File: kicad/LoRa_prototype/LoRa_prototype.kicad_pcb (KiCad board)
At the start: 4 copper layers, 100 x 90 mm, 138 parts, among them J1 Conn_ST_STDC14, J10 SYS, J11 BME, J12 GPS, J14 SPI_FLASH, J15 SYS, J18 MCO, J2 USB_C_Receptacle_PowerOnly_6P, J3 BAT, J4 SMA Female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

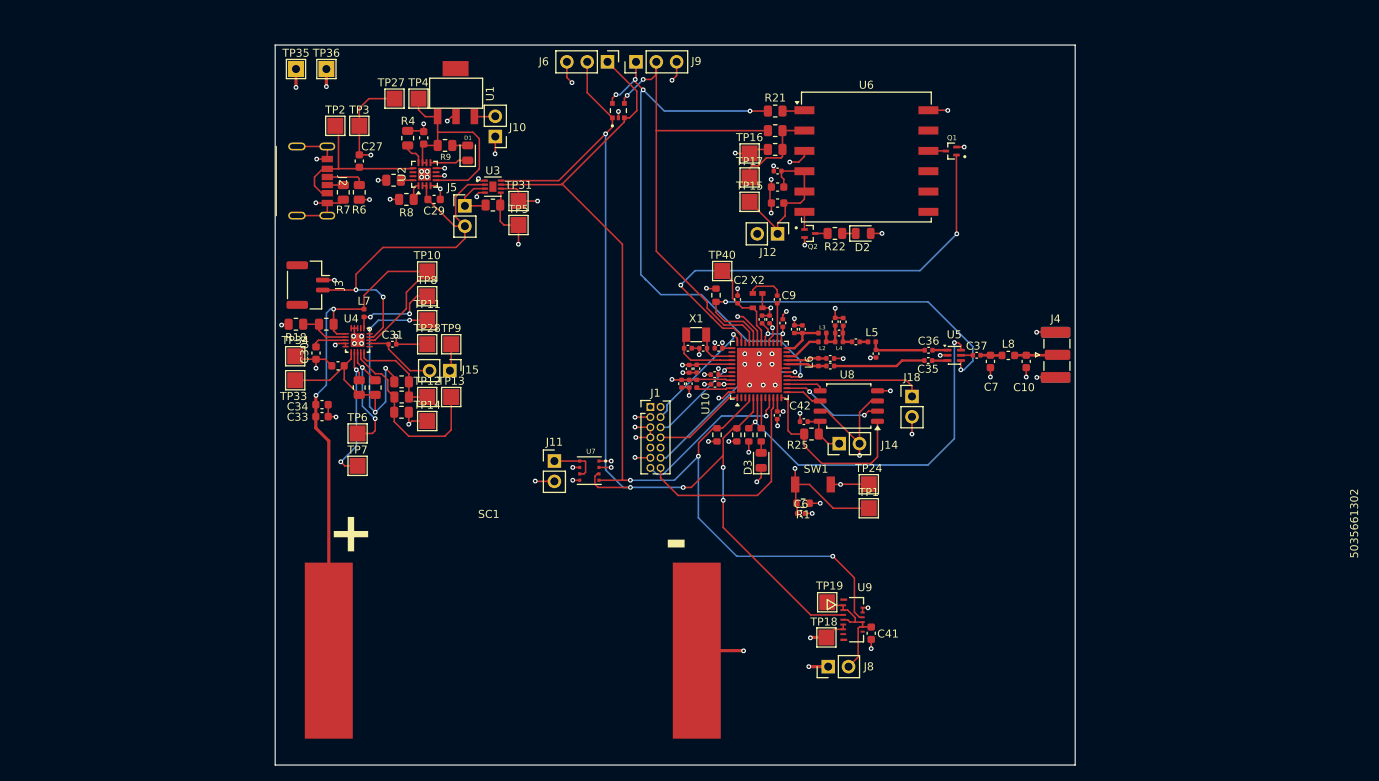
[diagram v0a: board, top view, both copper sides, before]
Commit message: Prettified silkscreen layer
0 errors and 33 warnings in DRC
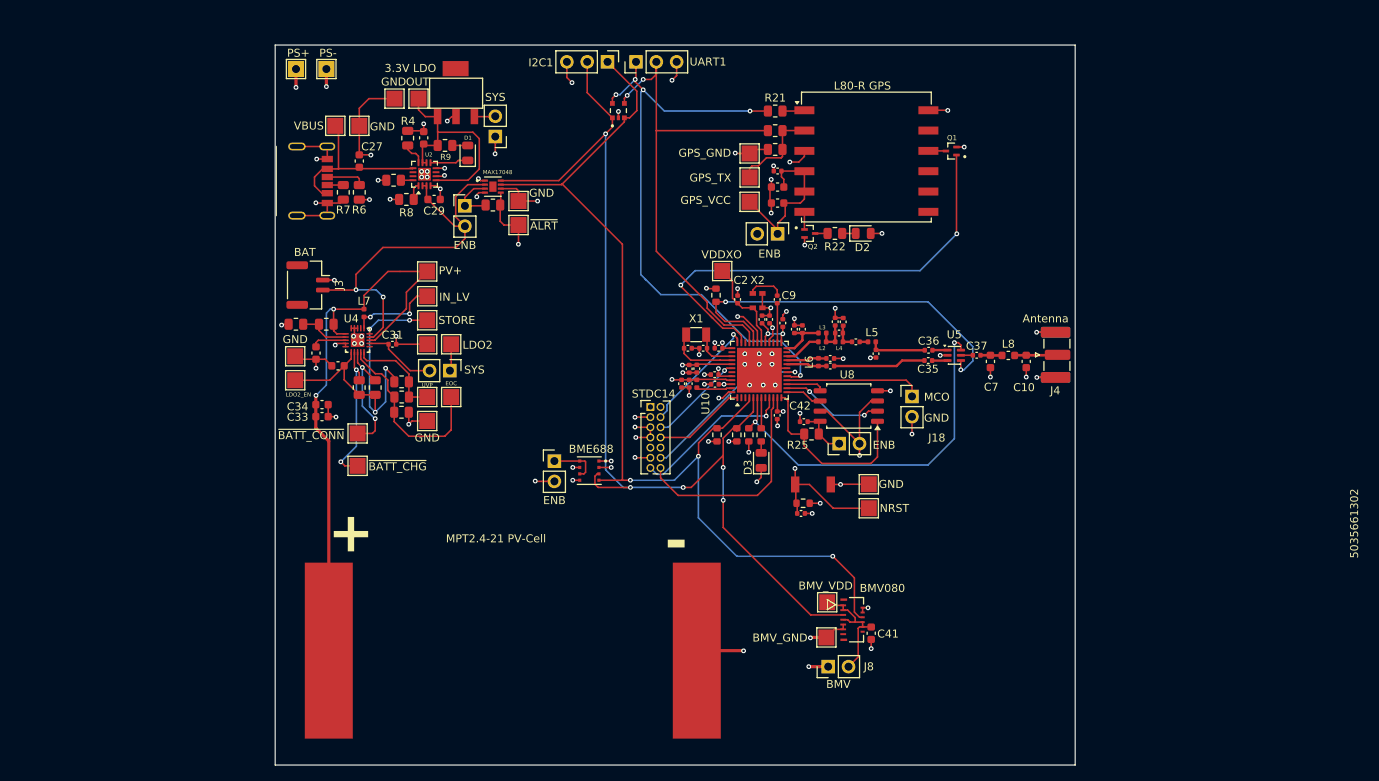
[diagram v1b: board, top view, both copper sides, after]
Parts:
- J1: value Conn_ST_STDC14 -> STDC14
- J11: value BME -> ENB
- J12: value GPS -> ENB
- J14: value SPI_FLASH -> ENB
- J4: value SMA Female -> Antenna
- J5: value FG -> ENB
- SC1: value PV_Cell -> MPT2.4-21 PV-Cell
- TP4: value BQ_OUT -> OUT
- U1: value TC1262-33 -> 3.3V LDO
- U6: value L80-R -> L80-R GPS
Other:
- board text added: "GND"

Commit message: Done layout (Milestone)
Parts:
- J8: value BMV -> ENB
- moved TP19 2.42 mm to (157.1, 132.5)
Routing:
- net Net-(J8-Pin_2): track 15.4 -> 21.4 mm
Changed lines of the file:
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@@
 			(at 0 5.075 180)
 			(layer "F.SilkS")
+			(hide yes)
 			(effects
 				(font
@@
 			)
 		)
-		(property "Value" "BMV"
-			(at -2.2 1.275 180)
+		(property "Value" "ENB"
+			(at -0.2 5.775 180)
 			(layer "F.SilkS" knockout)
 			(effects
@@
 		(tags "QFN NoLead ST_UFQFPN48 Analog_CP-48-13 JEDEC_MO-220-WKKD-4")
 		(property "Reference" "U10"
-			(at -4.178521 -6.723511 90)
+			(at 4.946479 -1.223511 180)
 			(layer "F.SilkS")
 			(effects
@@
 		)
 		(property "Value" "GND"
-			(at 2.8875 -1 0)
+			(at 2.7875 1 0)
 			(layer "F.SilkS")
 			(effects
@@
 	(footprint "TestPoint:TestPoint_Pad_2.0x2.0mm"
 		(layer "F.Cu")
-		(at 158 134.75 -90)
+		(at 157.1 132.5 -90)
 		(descr "SMD rectangular pad as test Point, square 2.0mm side length")
 		(tags "test point SMD pad rectangle square")
@@
 		)
 		(property "Value" "NRST"
-			(at 0 2.32 0)
+			(at -0.025 -1.625 0)
 			(unlocked yes)
-			(layer "F.Fab")
+			(layer "F.SilkS" knockout)
 			(effects
 				(font
-					(size 1 1)
+					(size 0.8 0.8)
 					(thickness 0.15)
 				)
@@
 	)
 	(segment
+		(start 160.000613 135.135947)
+		(end 160.560613 135.135947)
+		(width 0.2)
+		(layer "F.Cu")
+		(net "Net-(J8-Pin_2)")
+	)
+	(segment
 		(start 161.5 136.675334)
 		(end 161.5 137.23095)
@@
 	)
 	(segment
+		(start 161 133.3)
+		(end 160.2 132.5)
+		(width 0.2)
+		(layer "F.Cu")
+		(net "Net-(J8-Pin_2)")
+	)
+	(segment
 		(start 160.85562 137.23095)
 		(end 161.5 137.23095)
@@
 	)
 	(segment
-		(start 161.870613 141.594387)
-		(end 161.870613 138.005947)
+		(start 157.1 132.5)
+		(end 157.1 133.85)
 		(width 0.2)
 		(layer "F.Cu")
@@
 	)
 	(segment
-		(start 158 134.75)
-		(end 158.385947 135.135947)
+		(start 160.560613 135.135947)
+		(end 161 134.69656)
+		(width 0.2)
+		(layer "F.Cu")
+		(net "Net-(J8-Pin_2)")
+	)
+	(segment
+		(start 161.870613 141.594387)
+		(end 161.870613 138.005947)
 		(width 0.2)
 		(layer "F.Cu")
@@
 	)
 	(segment
-		(start 158.385947 135.135947)
-		(end 160.000613 135.135947)
+		(start 160.2 132.5)
+		(end 157.1 132.5)
 		(width 0.2)
 		(layer "F.Cu")
@@
 	)
 	(segment
+		(start 161 134.69656)
+		(end 161 133.3)
+		(width 0.2)
+		(layer "F.Cu")
+		(net "Net-(J8-Pin_2)")
+	)
+	(segment
 		(start 162.430613 137.830949)
 		(end 163.480949 137.830949)
@@
 		(members "00b88854-e0c5-48ce-b528-49b20548801e" "03d87a8a-3d7e-410a-8e2b-49f913e4700b"
 			"055845d4-aa3c-458b-b670-a7816f63b458" "062f0187-22d9-4161-a9bd-db5cf0b00279"
-			"08019439-ae15-4e6e-9966-5ae4cb823c61" "0e3633f3-5b09-4bdc-8659-46b67b607819"
+			"07f98a1d-b8b9-4188-bec3-efa45987d172" "08019439-ae15-4e6e-9966-5ae4cb823c61"
+			"085cffdf-96f6-443a-bde2-12ab2cff61fc" "0e3633f3-5b09-4bdc-8659-46b67b607819"
 			"11aea62e-4604-424a-b3e9-4dfd25fff43e" "187c9432-41a9-4de3-b672-5d93e34af146"
 			"1ae718b5-574f-4813-b8db-fc4e22bc7677" "1db30650-b046-46c8-957e-cf9e743b56df"
 			"1fd0ceec-c4bd-451e-90b9-3aa4e1401383" "23858227-c49f-4699-818e-aaed916f56df"
 			"28304f72-98b4-47ac-b5e5-f7391cbf7274" "2a3b31d7-64ee-44f3-9aba-9836ea90b057"
+			"2a66b8c0-9121-41c7-8ee1-e7b0361b45c7" "2c5dd03a-7c1c-4822-8ebc-7a20dc650459"
 			"2edca70c-b7a2-45ce-b82c-2dff0ad44395" "32b4d137-7edd-4083-bc96-557bc44032df"
 			"33203de6-4eb6-4b51-8265-064324d23961" "3ed247ac-c773-46bc-96f1-3a706e972048"
 			"4ff9f230-0aed-4912-934b-fec5a1d5c0a0" "552a20f8-299b-45cc-bdff-f4f932ffb814"
-			"596db315-1186-410f-8a22-c09f5b604d0f" "6971085f-098d-4b86-9fee-b469335c6b80"
-			"6d6caf39-2102-4dc7-a04c-aa733859fc59" "6dde47d0-603e-40d9-9744-987b2f1cd7b7"
-			"6fea2eb8-18d7-488c-8147-031538d38619" "71d62618-2a64-4791-9483-66291f807fa6"
-			"7831691c-6a2e-41db-98f8-4c0c557ab2fe" "79a160ef-86dc-4b7e-b14b-f55a100a75c9"
-			"8019255c-e7a0-4c98-b36e-af0026a842d5" "8094239b-862c-462e-8a9f-f4b89e9ff72c"
-			"878316fc-df39-440d-be7f-d82de48aaf99" "8786f720-ffb5-4595-aa78-426151092c1e"
-			"980075ab-390d-4ac8-bf31-4729e4867b40" "9849b26f-ea98-4eab-989d-fa4010a3d4a6"
+			"6971085f-098d-4b86-9fee-b469335c6b80" "6d6caf39-2102-4dc7-a04c-aa733859fc59"
+			"6dde47d0-603e-40d9-9744-987b2f1cd7b7" "6fea2eb8-18d7-488c-8147-031538d38619"
+			"71d62618-2a64-4791-9483-66291f807fa6" "7831691c-6a2e-41db-98f8-4c0c557ab2fe"
+			"79a160ef-86dc-4b7e-b14b-f55a100a75c9" "8019255c-e7a0-4c98-b36e-af0026a842d5"
+			"8094239b-862c-462e-8a9f-f4b89e9ff72c" "878316fc-df39-440d-be7f-d82de48aaf99"
+			"8786f720-ffb5-4595-aa78-426151092c1e" "980075ab-390d-4ac8-bf31-4729e4867b40"
 			"9ba92ddb-2668-4540-8ff9-b1a3e865a2a1" "9fa939a9-ec2d-4f32-8412-a77670e36986"
 			"a87abfbc-a00c-4692-988e-4c722575bf59" "b90b7ee9-04a1-4f9e-b1c8-c81a9e7a0675"
-			"c245706f-6b97-4ec5-9eea-8f0735eecca9" "c60f20bf-98cc-45cf-85ff-06c4d46ee515"
-			"c80dbc9a-96b0-4921-9797-cd86b6c8647f" "ceb076f6-c45c-4e61-a4c0-7ac9ff2db899"
+			"be8ac290-4144-42f9-8fbc-b3c755e10dda" "c245706f-6b97-4ec5-9eea-8f0735eecca9"
+			"c60f20bf-98cc-45cf-85ff-06c4d46ee515" "c80dbc9a-96b0-4921-9797-cd86b6c8647f"
+			"ceb076f6-c45c-4e61-a4c0-7ac9ff2db899" "d4033e32-afc2-4d7a-b96b-0e904f83830c"
 			"d6a7aa3a-f3d7-4275-8c5a-33ac0569c92c" "d96d3098-cc7b-4503-95af-29d04b1d30b7"
 			"de7d2572-bd0d-4dae-8042-149d766ff0c3" "df0bbe26-9669-4912-bb5a-5dfc6c923c59"

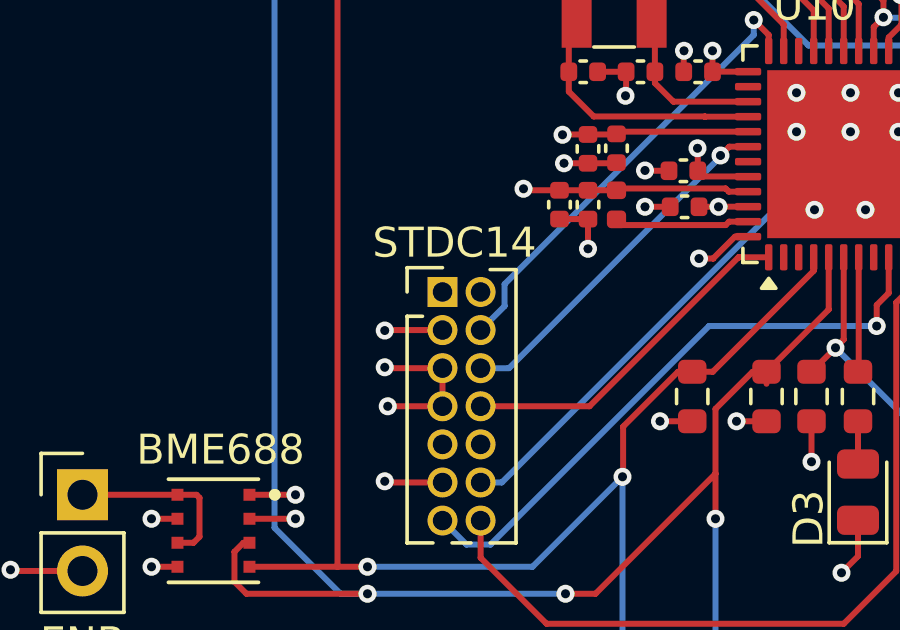
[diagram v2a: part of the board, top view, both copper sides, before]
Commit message: Added part numbers for JLCPCB (90% done)
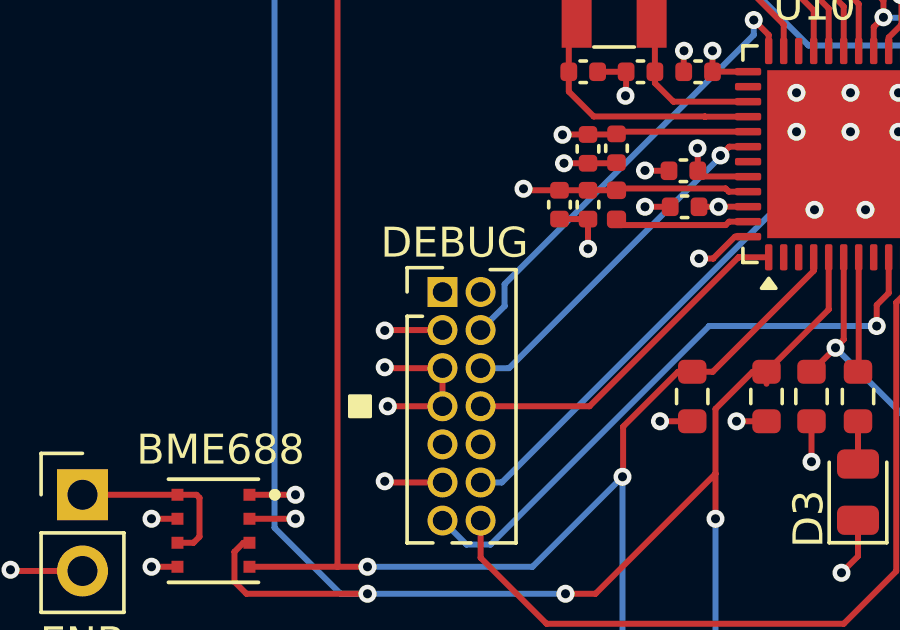
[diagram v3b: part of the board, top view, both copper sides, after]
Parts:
- J1: value STDC14 -> DEBUG

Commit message: Stable commit (22 DRC warnings only)
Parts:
- removed U10: STM32WL54CCUx, Package_DFN_QFN:QFN-48-1EP_7x7mm_P0.5mm_EP5.6x5.6mm
- added U11: STM32WL55CCUx, Package_DFN_QFN:QFN-48-1EP_7x7mm_P0.5mm_EP5.6x5.6mm, F.Cu at (149.5, 105.8)
- C4, C8: value 12.5pF -> 18pF
- J1: value DEBUG -> Conn_ST_STDC14
- J11: value ENB -> BME
- J12: value ENB -> GPS
- J14: value ENB -> SPI_FLASH
- J4: value Antenna -> SMA Female
- J5: value ENB -> FG
- J8: value ENB -> BMV
- SC1: value MPT2.4-21 PV-Cell -> PV_Cell
- TP4: value OUT -> BQ_OUT
- U1: value 3.3V LDO -> TC1262-33
- U6: value L80-R GPS -> L80-R
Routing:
- net Net-(J8-Pin_2): track 21.4 -> 20.0 mm
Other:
- board text added: "3.3V LDO"
- board text added: "ANTENNA"
- board text added: "DEBUG"
- board text added: "ENB"
- board text added: "OUT"

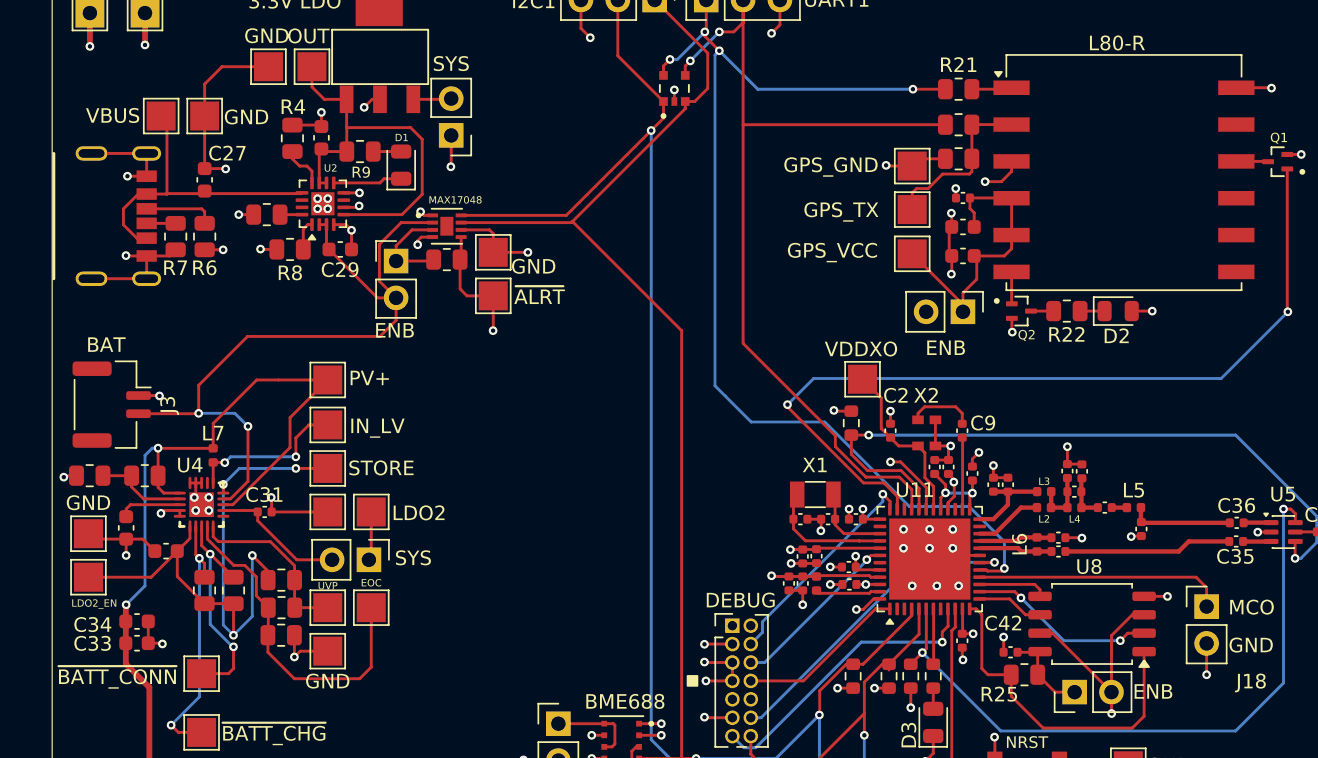
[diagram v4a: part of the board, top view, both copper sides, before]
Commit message: Added tear drops + tapered tracks
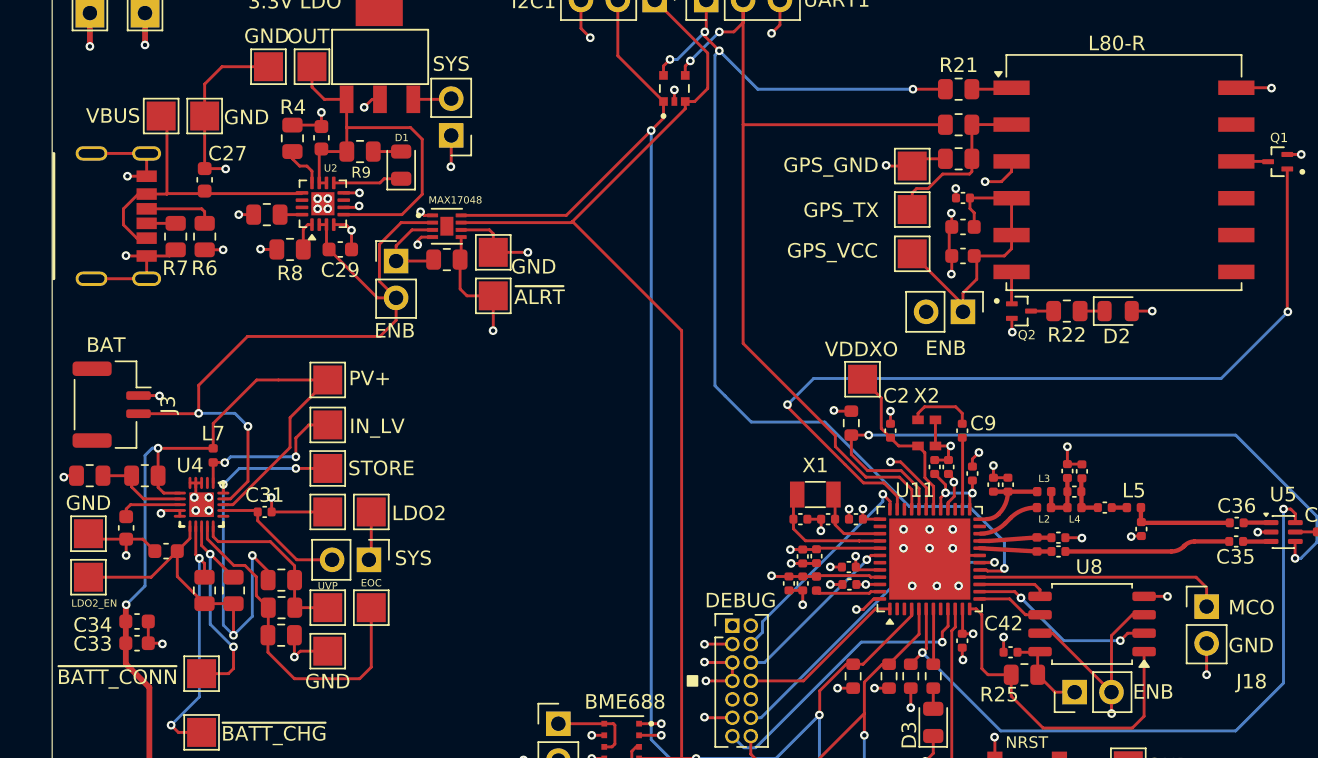
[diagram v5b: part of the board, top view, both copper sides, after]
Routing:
- net /POWER/STORE: track 45.8 -> 44.6 mm
- net /MCU/VR_PA: track 6.35 -> 5.75 mm

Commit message: Added manufacturing files
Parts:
- added G***: LOGO, LOGO, F.Cu at (121.5, 109.6)
- added G***: LOGO, LOGO, F.Cu at (174.3, 148.3)
- added G***: LOGO, LOGO, B.Cu at (117.9, 140.2)
- moved C41 3.88 mm to (163.5, 142.5)
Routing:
- net Net-(J8-Pin_2): track 20.0 -> 21.9 mm
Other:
- outline, holes or cut-outs redrawn
- board text added: "${ISSUE_DATE}"
- board text added: "${PROJECTNAME}"
- board text added: "${REVISION}"
- board text added: "3mm"
- board text added: "Board size: 90x100mm"
- board text added: "FAILED"
- board text added: "FLASHED"
- board text added: "Github link"
- board text added: "Hole is located at -30mm and 4mm relative to bottom right corner"
- board text added: "Hole is located at -35mm and 3mm relative to bottom left corner"
- board text added: "JLCJLCJLCJLC"
- board text added: "M3"
- board text added: "PASSED"
- board text added: "REV A"

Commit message: BOM consolidation
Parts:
- added C32: 47uF, Capacitor_SMD:C_0805_2012Metric, F.Cu at (116.0, 99.5)
- C13, C18: footprint Capacitor_SMD:C_0402_1005Metric -> Capacitor_SMD:C_0603_1608Metric
- R11, R12: value 10M -> 1M
- R13: value 6.2M -> 1M
- R14: value 500K -> 82K
- R15: value 2.7M -> 470K
- R17: value 1.5M -> 200K
- R18: value 8.2M -> 1M
- R4: value 1.8K -> 2K
- moved C13 1.63 mm to (138.2, 107.0), turned to 180 degrees
- moved C18 0.38 mm to (153.7, 100.3)
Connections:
- U2 pad 17: GND -> (no net)
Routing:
- net /POWER/STORE: track 44.6 -> 51.6 mm
- net GND: track 175.4 -> 178.2 mm, vias 87 -> 90
- net /MCU/VFBSMPS: track 28.7 -> 28.3 mm, vias 3 -> 2
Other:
- board text removed: "${REVISION}"
